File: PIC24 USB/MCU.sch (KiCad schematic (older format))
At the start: 12 parts, among them U1 PIC24FJXXXGB106, X1 CRYSTAL_12MHZ

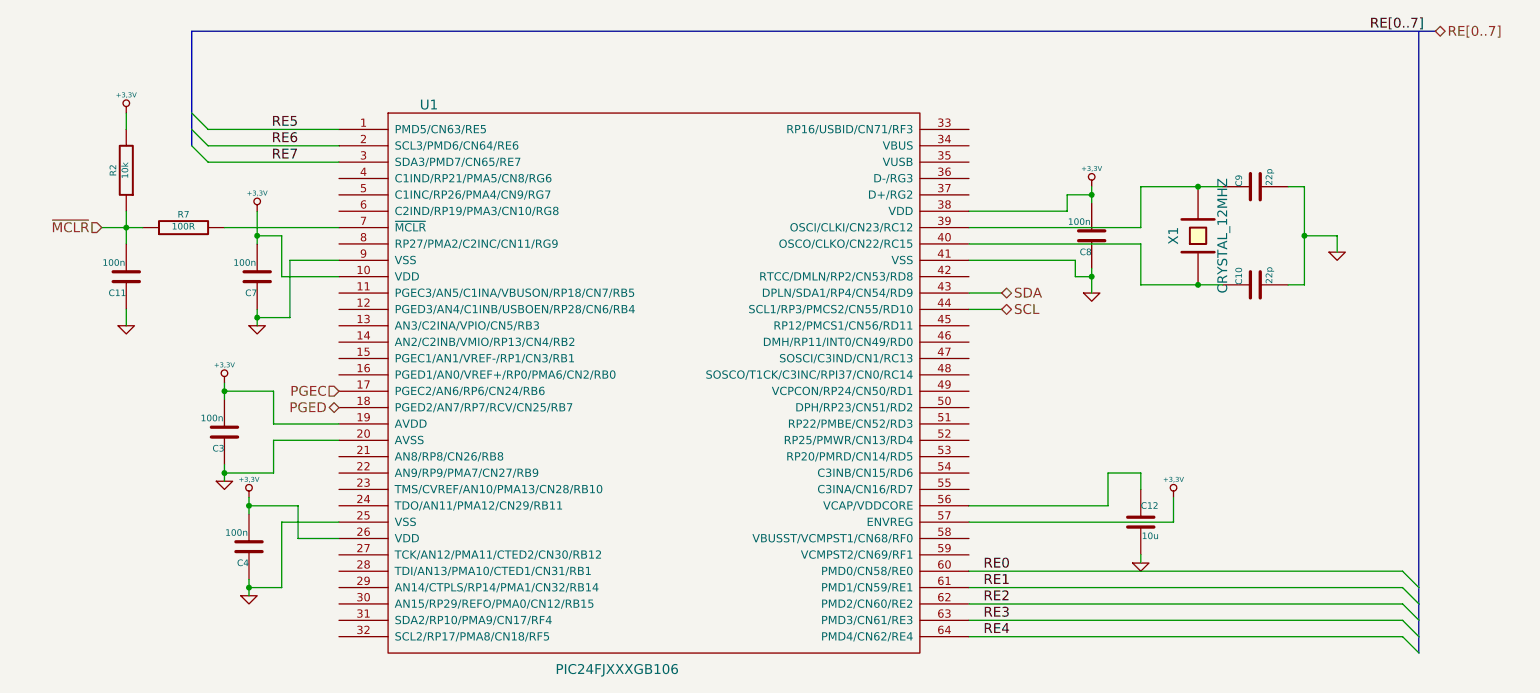
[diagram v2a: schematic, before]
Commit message: converted kicad project for newer version from kicad.nosoftware.cz
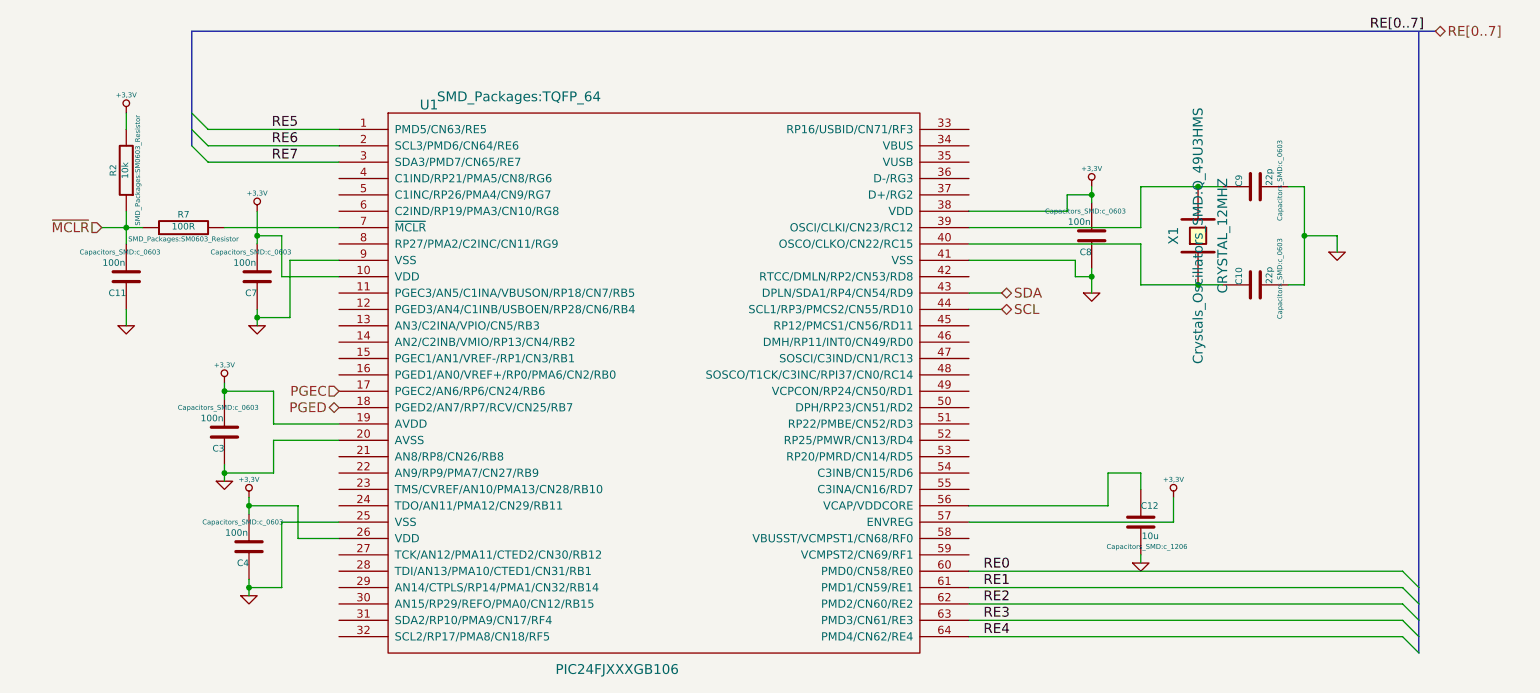
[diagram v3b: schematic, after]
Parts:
- C10, C11, C3, C4, C7, C8, C9: footprint ~ -> Capacitors_SMD:c_0603
- C12: footprint ~ -> Capacitors_SMD:c_1206
- R2, R7: footprint ~ -> SMD_Packages:SM0603_Resistor
- U1: footprint ~ -> SMD_Packages:TQFP_64
- X1: footprint ~ -> Crystals_Oscillators_SMD:Q_49U3HMS
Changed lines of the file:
@@
-EESchema Schematic File Version 2  date 03.08.2014 21:39:24
+EESchema Schematic File Version 2
 LIBS:power
 LIBS:device
@@
 LIBS:microchip_hele
 LIBS:PIC24_USB_IR_Transmitter-cache
-EELAYER 27 0
+EELAYER 24 0
 EELAYER END
 $Descr A4 11693 8268
@@
 F 0 "X1" H 8700 3100 60  0000 C CNN
 F 1 "CRYSTAL_12MHZ" H 8700 2800 60  0000 C CNN
-F 2 "~" H 8700 2950 60  0000 C CNN
+F 2 "Crystals_Oscillators_SMD:Q_49U3HMS" H 8700 2950 60  0000 C CNN
 F 3 "~" H 8700 2950 60  0000 C CNN
 	1    8700 2950
@@
 F 0 "C9" H 9050 2750 40  0000 L CNN
 F 1 "22p" H 9056 2565 40  0000 L CNN
-F 2 "~" H 9088 2500 30  0000 C CNN
+F 2 "Capacitors_SMD:c_0603" H 9088 2500 30  0000 C CNN
 F 3 "~" H 9050 2650 60  0000 C CNN
 	1    9050 2650
@@
 F 0 "C10" H 9050 3350 40  0000 L CNN
 F 1 "22p" H 9056 3165 40  0000 L CNN
-F 2 "~" H 9088 3100 30  0000 C CNN
+F 2 "Capacitors_SMD:c_0603" H 9088 3100 30  0000 C CNN
 F 3 "~" H 9050 3250 60  0000 C CNN
 	1    9050 3250
@@
 F 0 "C3" H 2750 4250 40  0000 L CNN
 F 1 "100n" H 2756 4065 40  0000 L CNN
-F 2 "~" H 2788 4000 30  0000 C CNN
+F 2 "Capacitors_SMD:c_0603" H 2788 4000 30  0000 C CNN
 F 3 "~" H 2750 4150 60  0000 C CNN
 	1    2750 4150
@@
 F 0 "C4" H 2900 4950 40  0000 L CNN
 F 1 "100n" H 2906 4765 40  0000 L CNN
-F 2 "~" H 2938 4700 30  0000 C CNN
+F 2 "Capacitors_SMD:c_0603" H 2938 4700 30  0000 C CNN
 F 3 "~" H 2900 4850 60  0000 C CNN
 	1    2900 4850
@@
 F 0 "C7" H 2950 3300 40  0000 L CNN
 F 1 "100n" H 2956 3115 40  0000 L CNN
-F 2 "~" H 2988 3050 30  0000 C CNN
+F 2 "Capacitors_SMD:c_0603" H 2988 3050 30  0000 C CNN
 F 3 "~" H 2950 3200 60  0000 C CNN
 	1    2950 3200
@@
 F 0 "C8" H 8050 3050 40  0000 L CNN
 F 1 "100n" H 8056 2865 40  0000 L CNN
-F 2 "~" H 8088 2800 30  0000 C CNN
+F 2 "Capacitors_SMD:c_0603" H 8088 2800 30  0000 C CNN
 F 3 "~" H 8050 2950 60  0000 C CNN
 	1    8050 2950
@@
 F 0 "C12" H 8350 4800 40  0000 L CNN
 F 1 "10u" H 8356 4615 40  0000 L CNN
-F 2 "~" H 8388 4550 30  0000 C CNN
+F 2 "Capacitors_SMD:c_1206" H 8388 4550 30  0000 C CNN
 F 3 "~" H 8350 4700 60  0000 C CNN
 	1    8350 4700
@@
 F 0 "U1" H 4000 2050 60  0000 C CNN
 F 1 "PIC24FJXXXGB106" H 5150 -1400 60  0000 C CNN
-F 2 "~" H 4550 2100 60  0000 C CNN
+F 2 "SMD_Packages:TQFP_64" H 4550 2100 60  0000 C CNN
 F 3 "~" H 4550 2100 60  0000 C CNN
 	1    4550 2100
@@
 F 0 "R7" V 2580 2900 40  0000 C CNN
 F 1 "100R" V 2507 2901 40  0000 C CNN
-F 2 "~" V 2430 2900 30  0000 C CNN
+F 2 "SMD_Packages:SM0603_Resistor" V 2430 2900 30  0000 C CNN
 F 3 "~" H 2500 2900 30  0000 C CNN
 	1    2500 2900
@@
 F 0 "R2" V 2230 2550 40  0000 C CNN
 F 1 "10k" V 2157 2551 40  0000 C CNN
-F 2 "~" V 2080 2550 30  0000 C CNN
+F 2 "SMD_Packages:SM0603_Resistor" V 2080 2550 30  0000 C CNN
 F 3 "~" H 2150 2550 30  0000 C CNN
 	1    2150 2550
@@
 F 0 "C11" H 2150 3300 40  0000 L CNN
 F 1 "100n" H 2156 3115 40  0000 L CNN
-F 2 "~" H 2188 3050 30  0000 C CNN
+F 2 "Capacitors_SMD:c_0603" H 2188 3050 30  0000 C CNN
 F 3 "~" H 2150 3200 60  0000 C CNN
 	1    2150 3200
